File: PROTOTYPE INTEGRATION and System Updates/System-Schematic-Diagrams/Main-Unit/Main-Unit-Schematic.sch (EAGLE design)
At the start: 15 parts, among them U1 MSP430FR2110IPW16, U2 MCP6022-I/P, U3 L7805CV, U4 TMP36GT9ZT_3_ADI

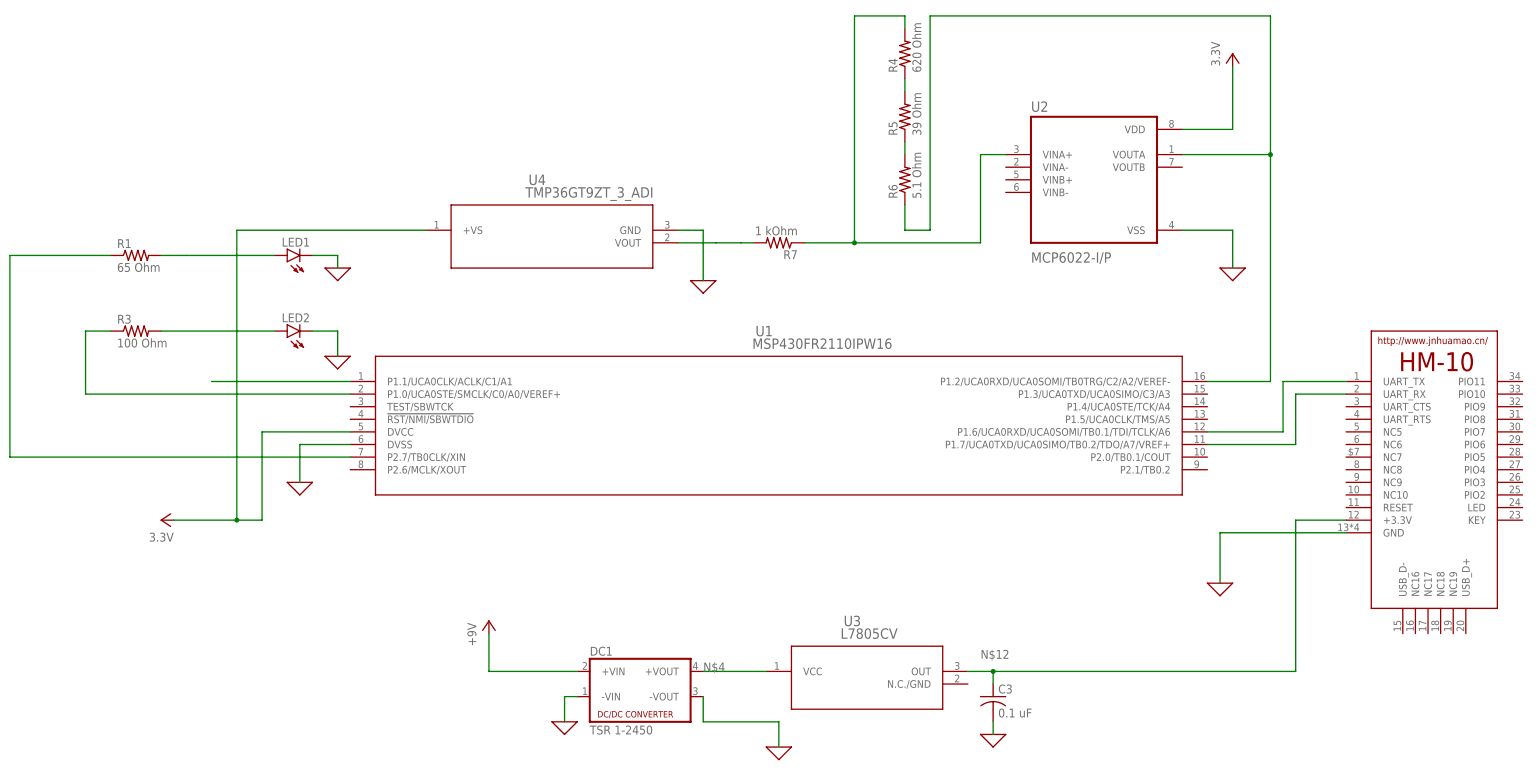
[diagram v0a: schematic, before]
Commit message: Updated Schematics and BOM
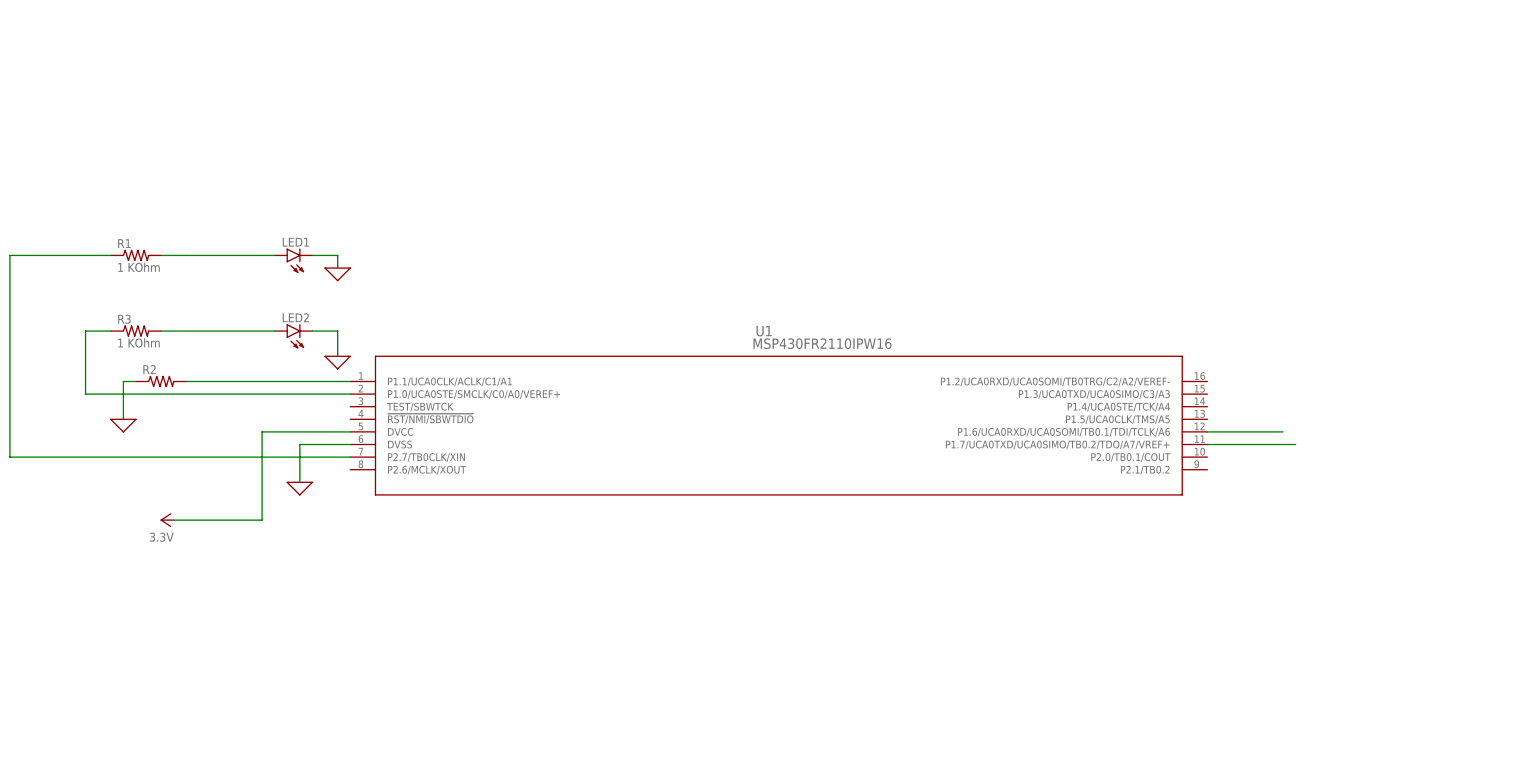
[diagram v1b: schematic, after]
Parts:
- removed C3: 0.1 uF, rcl:C-US050-024X044
- removed DC1: TSR 1-2450, dc-dc-converter:NME
- removed E1: HM-10-BOARD, HM-10:HM-10-BOARD
- removed R4: 620 Ohm, rcl:R-US_0204/7
- removed R5: 39 Ohm, rcl:R-US_0204/7
- removed R6: 5.1 Ohm, rcl:R-US_0204/7
- removed R7: 1 kOhm, rcl:R-US_0204/7
- removed U2: MCP6022-I/P, MCP6022-I_P:MCP6022-I/P
- removed U3: L7805CV, 2023-03-08_12-17-23_Library:BA033CC0FP-E2TO252-3_ROM
- removed U4: TMP36GT9ZT_3_ADI, 2023-03-28_14-12-25_Library:TMP36GT9ZT_3_ADI
- added R2: (no value), rcl:R-US_0204/7
- R1: value 65 Ohm -> 1 KOhm
- R3: value 100 Ohm -> 1 KOhm
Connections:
- removed net +5V: DC1.+VIN
- removed net N$10: R6.1, U1.P1.2/UCA0RXD/UCA0SOMI/TB0TRG/C2/A2/VEREF-, U2.VOUTA
- removed net N$11: R4.2, R7.1, U2.VINA+
- removed net N$12: C3.1, E1.+3.3V, R7.2, U3.OUT, U4.VOUT
- removed net N$8: R4.1, R5.2
- removed net N$9: R5.1, R6.2
- net 0: now also R2.1; no longer C3.2, DC1.-VIN, DC1.-VOUT, E1.GND, U2.VSS, U4.GND
- net N$1: no longer E1.UART_TX
- net N$2: no longer E1.UART_RX
- net N$3: now also R2.2
- net N$4: no longer DC1.+VOUT, U3.VCC
- net VCC: no longer U2.VDD, U4.+VS
